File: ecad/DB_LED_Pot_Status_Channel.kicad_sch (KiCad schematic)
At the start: 34 parts, among them J8 B6B-XH-A(LF)(SN), SW1 KSC_SLT_241G_LFS

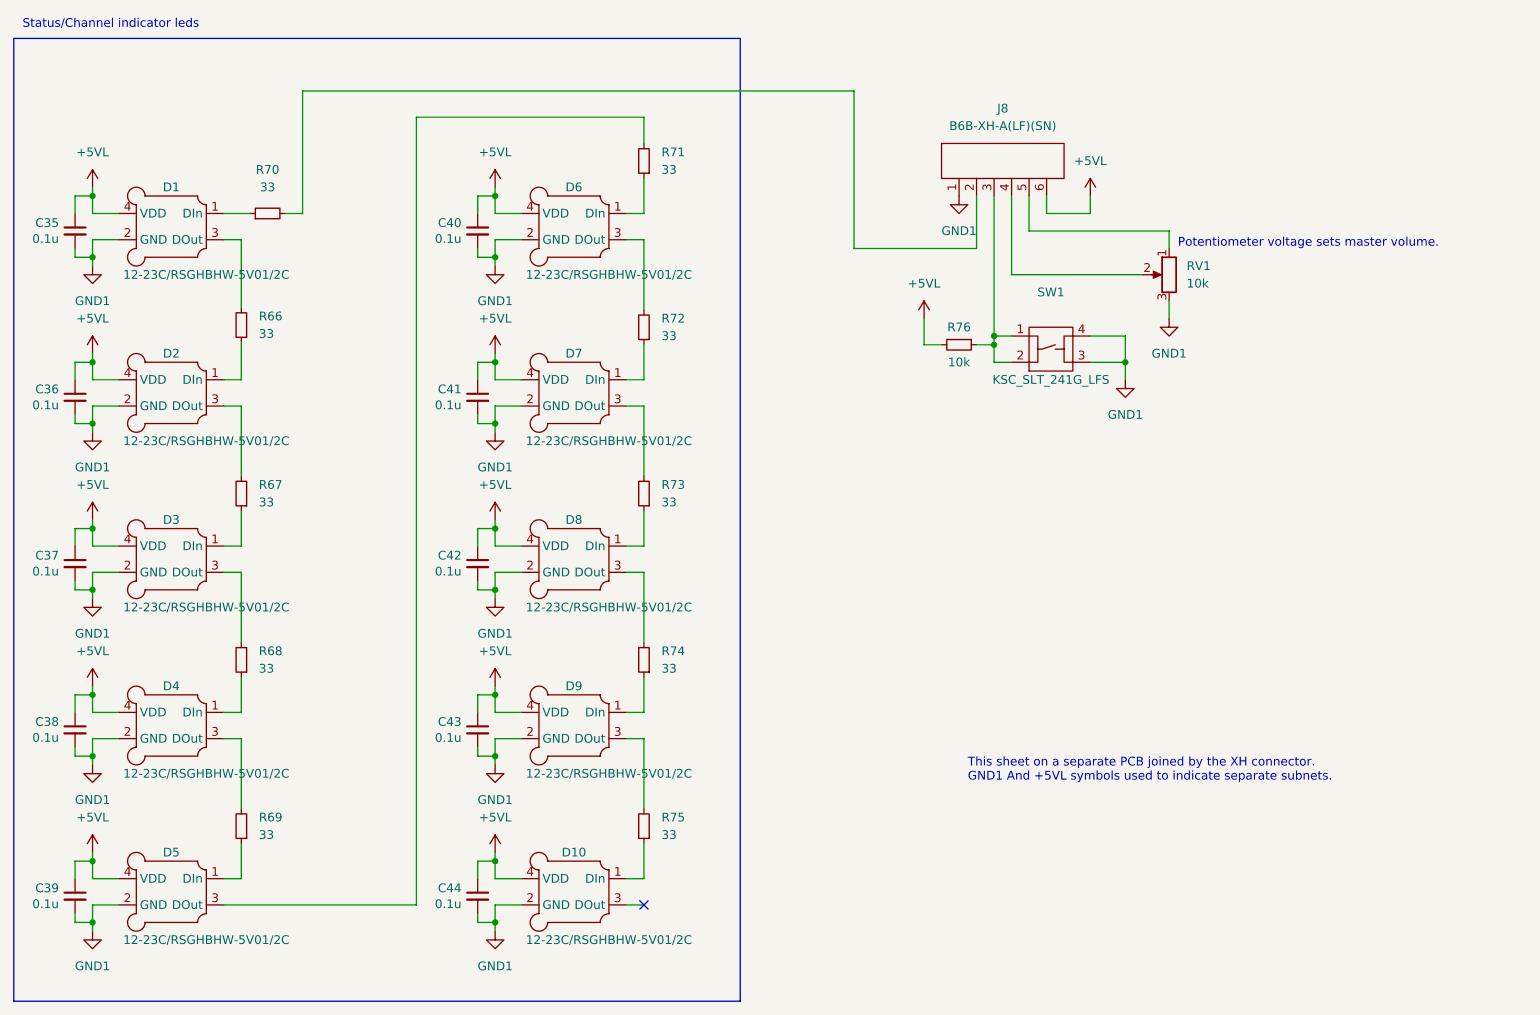
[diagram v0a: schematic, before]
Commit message: Update to Kicad 7 and generate PDF schematic.
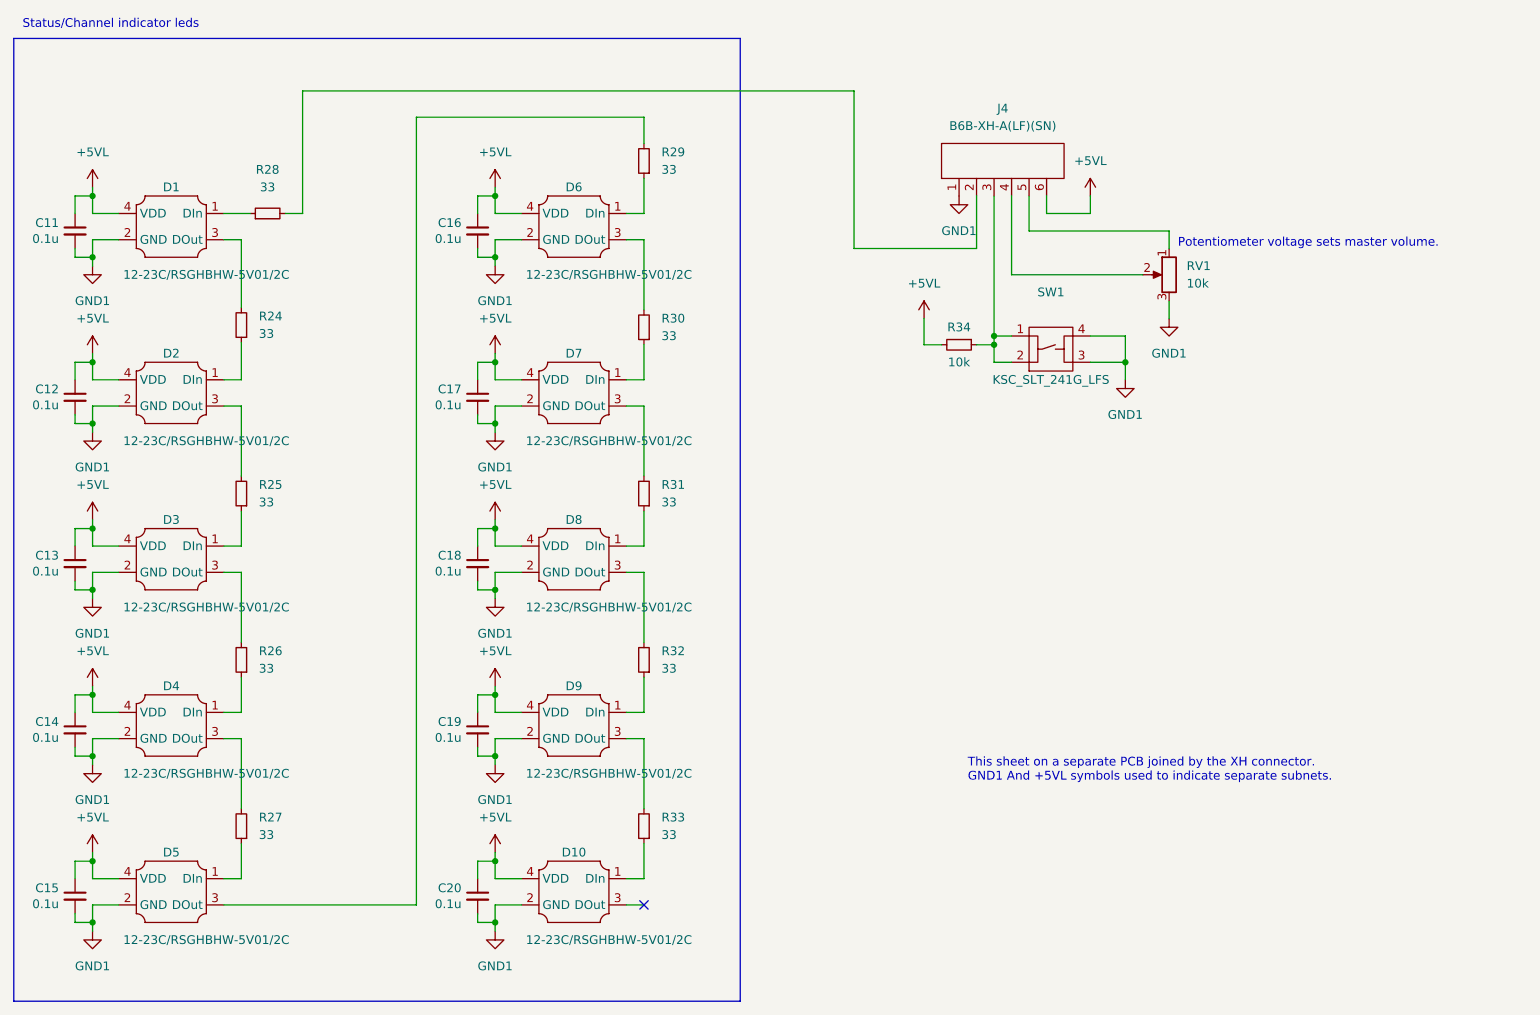
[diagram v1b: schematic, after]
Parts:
- renumbered C35 to C11, C36 to C12, C37 to C13, C38 to C14, C39 to C15, C40 to C16, C41 to C17, C42 to C18, C43 to C19, C44 to C20, J8 to J4, R66 to R24, R67 to R25, R68 to R26, R69 to R27, R70 to R28, R71 to R29, R72 to R30, R73 to R31, R74 to R32, R75 to R33, R76 to R34

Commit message: Fixes to footprint numbering in multi-unit parts.
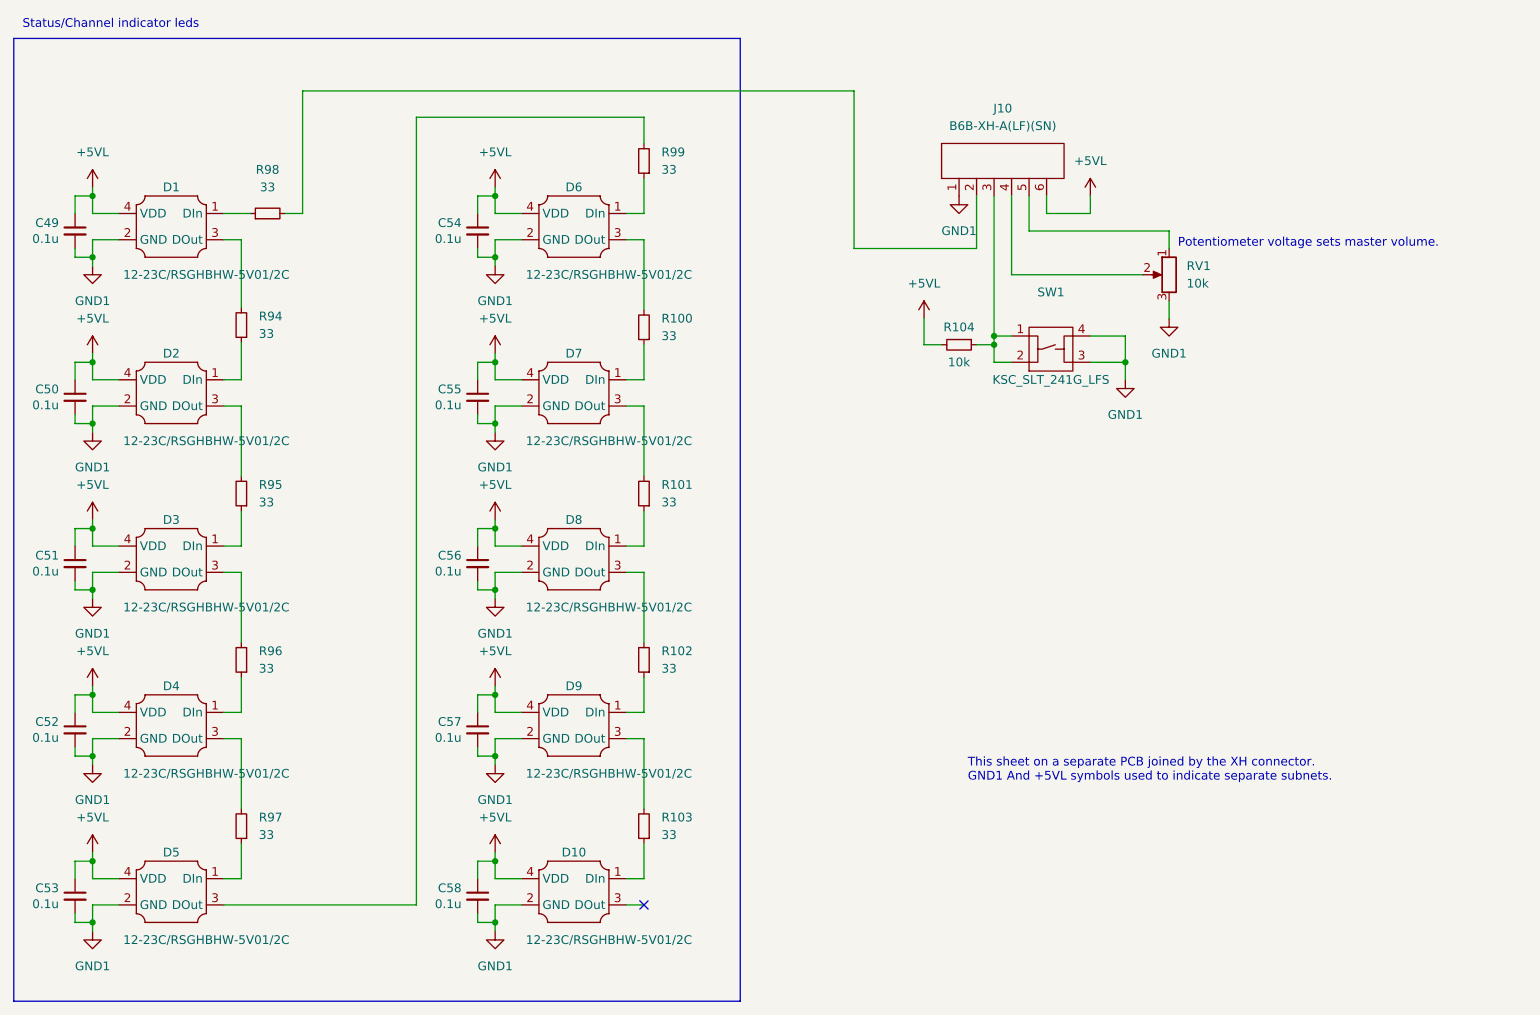
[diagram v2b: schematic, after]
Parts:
- renumbered C11 to C49, C12 to C50, C13 to C51, C14 to C52, C15 to C53, C16 to C54, C17 to C55, C18 to C56, C19 to C57, C20 to C58, J4 to J10, R30 to R100, R31 to R101, R32 to R102, R33 to R103, R34 to R104, R24 to R94, R25 to R95, R26 to R96, R27 to R97, R28 to R98, R29 to R99
